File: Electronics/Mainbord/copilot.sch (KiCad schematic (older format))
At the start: 22 parts, among them J33 Screw_Terminal_01x10, J34 Screw_Terminal_01x10, J35 Screw_Terminal_01x10, J36 Screw_Terminal_01x02, J37 Screw_Terminal_01x10, J38 Screw_Terminal_01x10, J39 Screw_Terminal_01x10, U45 74HC165, U46 74HC165, U47 74HC165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

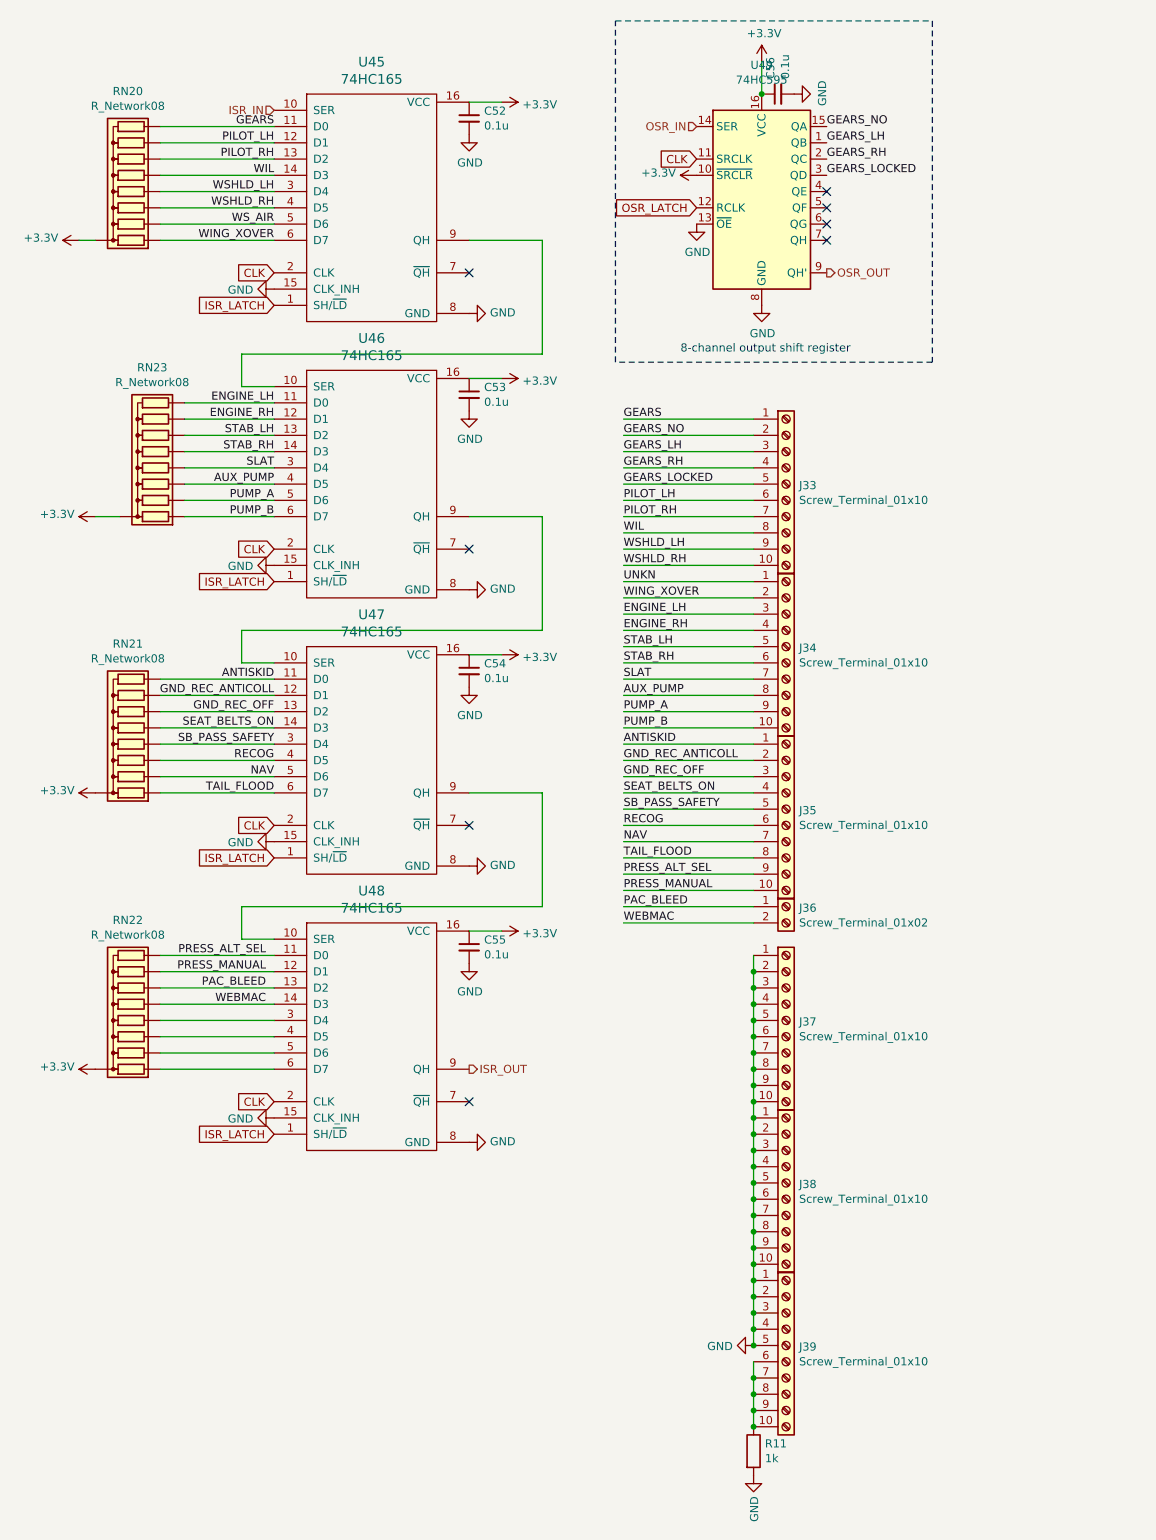
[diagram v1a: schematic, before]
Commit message: Electronics - Minor changes
Resistors to LEDs, transistors
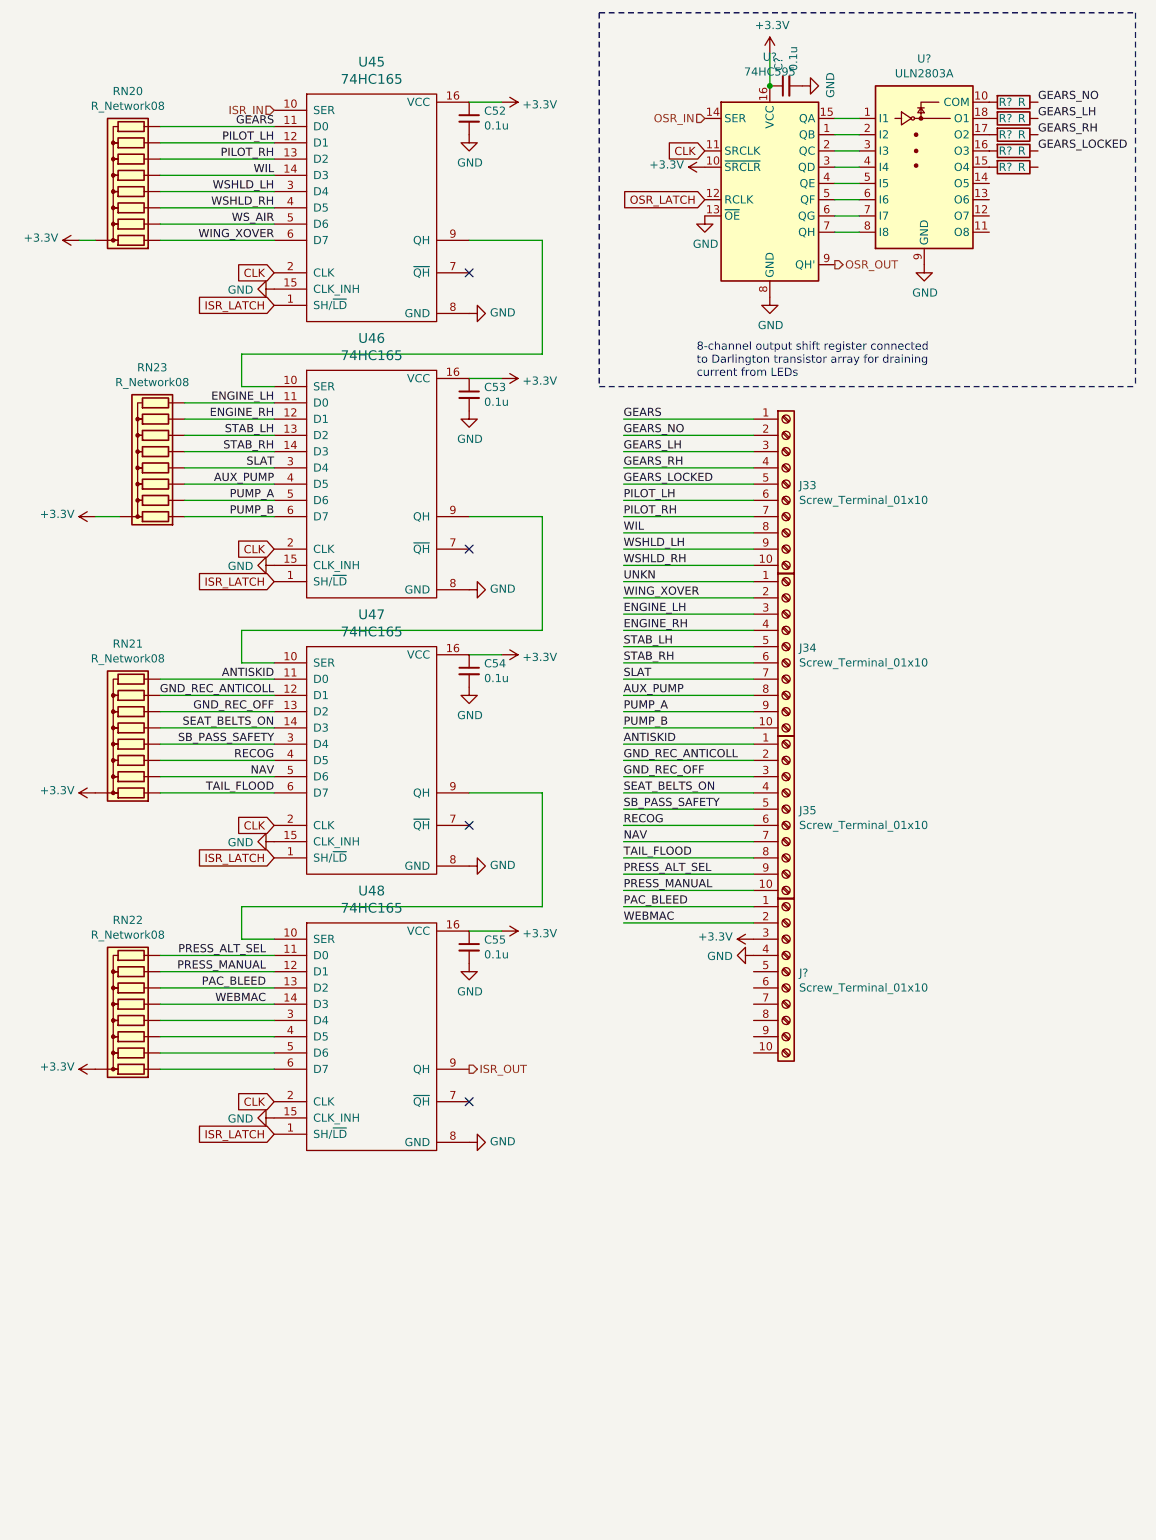
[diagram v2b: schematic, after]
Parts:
- removed C56: 0.1u, symbol Device:C_Small
- removed J36: Screw_Terminal_01x02, symbol Connector:Screw_Terminal_01x02
- removed J37, J38, J39: Screw_Terminal_01x10, symbol Connector:Screw_Terminal_01x10
- removed R11: 1k, symbol Device:R
- removed U49: 74HC595, symbol 74xx:74HC595
- added C?: 0.1u, symbol Device:C_Small
- added J?: Screw_Terminal_01x10, symbol Connector:Screw_Terminal_01x10
- added R? (x5): R, symbol Device:R
- added U?: 74HC595, symbol 74xx:74HC595
- added U?: ULN2803A, symbol Transistor_Array:ULN2803A
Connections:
- net +3V3: now also C?.1, J?.3 (Pin_3), U?.10 (~SRCLR), U?.16 (VCC)
- net CLK: now also U?.11 (SRCLK)
- net GEARS_LH: now also R?.1
- net GEARS_LOCKED: now also R?.1
- net GEARS_NO: now also R?.1
- net GEARS_RH: now also R?.1
- net GND: now also C?.2, J?.4 (Pin_4), U?.13 (~OE), U?.8 (GND), U?.9 (GND)
- net OSR_IN: now also U?.14 (SER)
- net OSR_LATCH: now also U?.12 (RCLK)
- net OSR_OUT: now also U?.9 (QH')
- net PAC_BLEED: now also J?.1 (Pin_1)
- net WEBMAC: now also J?.2 (Pin_2)
- new net: U?.1 (QB), U?.2 (I2)
- new net: U?.1 (I1), U?.15 (QA)
- new net: U?.2 (QC), U?.3 (I3)
- new net: U?.3 (QD), U?.4 (I4)
- new net: U?.4 (QE), U?.5 (I5)
- new net: U?.5 (QF), U?.6 (I6)
- new net: U?.6 (QG), U?.7 (I7)
- new net: U?.7 (QH), U?.8 (I8)
- new net: R?.2, U?.10 (COM)
- new net: R?.2, U?.15 (O4)
- new net: R?.2, U?.16 (O3)
- new net: R?.2, U?.17 (O2)
- new net: R?.2, U?.18 (O1)
- no-connect marks 8 -> 4
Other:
- note added: "8-channel output shift register connected \nto Darlington transistor array for draining \ncurrent from LEDs"
- note removed: "8-channel output shift register"

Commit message: Electronics - Misc works
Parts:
- R? (x4): value R -> 68
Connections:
- net at U?.10 (COM): no longer R?.2
- net at U?.14 (O5): now also R?.2
- net at U?.15 (O4): now also R?.2; no longer R?.2
- net at U?.16 (O3): now also R?.2; no longer R?.2
- net at U?.17 (O2): now also R?.2; no longer R?.2
- net at U?.18 (O1): now also R?.2; no longer R?.2
- no-connect marks 4 -> 5
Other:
- moved on the sheet: R?
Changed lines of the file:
@@
 AR Path="/5DC174D4/5E02571A" Ref="C?"  Part="1"
 AR Path="/5DC31399/5E02571A" Ref="C?"  Part="1"
+AR Path="/5DC2EEA6/5E02571A" Ref="C?"  Part="1"
 F 0 "C?" H 5742 1246 50  0000 L CNN
 F 1 "0.1u" H 5742 1155 50  0000 L CNN
@@
 AR Path="/5DC174D4/5E025721" Ref="#PWR?"  Part="1"
 AR Path="/5DC31399/5E025721" Ref="#PWR?"  Part="1"
+AR Path="/5DC2EEA6/5E025721" Ref="#PWR?"  Part="1"
 F 0 "#PWR?" H 5750 950 50  0001 C CNN
 F 1 "GND" H 5755 1027 50  0000 C CNN
@@
 AR Path="/5DC174D4/5E025728" Ref="U?"  Part="1"
 AR Path="/5DC31399/5E025728" Ref="U?"  Part="1"
+AR Path="/5DC2EEA6/5E025728" Ref="U?"  Part="1"
 F 0 "U?" H 5550 2578 50  0000 C CNN
 F 1 "74HC595" H 5550 2487 50  0000 C CNN
@@
 AR Path="/5DC174D4/5E025730" Ref="#PWR?"  Part="1"
 AR Path="/5DC31399/5E025730" Ref="#PWR?"  Part="1"
+AR Path="/5DC2EEA6/5E025730" Ref="#PWR?"  Part="1"
 F 0 "#PWR?" H 5550 2250 50  0001 C CNN
 F 1 "GND" H 5555 2327 50  0000 C CNN
@@
 AR Path="/5DC174D4/5E025737" Ref="#PWR?"  Part="1"
 AR Path="/5DC31399/5E025737" Ref="#PWR?"  Part="1"
+AR Path="/5DC2EEA6/5E025737" Ref="#PWR?"  Part="1"
 F 0 "#PWR?" H 5150 1750 50  0001 C CNN
 F 1 "GND" H 5155 1827 50  0000 C CNN
@@
 AR Path="/5DC174D4/5E02573E" Ref="#PWR?"  Part="1"
 AR Path="/5DC31399/5E02573E" Ref="#PWR?"  Part="1"
+AR Path="/5DC2EEA6/5E02573E" Ref="#PWR?"  Part="1"
 F 0 "#PWR?" H 5550 850 50  0001 C CNN
 F 1 "+3.3V" H 5565 1173 50  0000 C CNN
@@
 AR Path="/5DC174D4/5E025744" Ref="#PWR?"  Part="1"
 AR Path="/5DC31399/5E025744" Ref="#PWR?"  Part="1"
+AR Path="/5DC2EEA6/5E025744" Ref="#PWR?"  Part="1"
 F 0 "#PWR?" H 5150 1550 50  0001 C CNN
 F 1 "+3.3V" V 5165 1828 50  0000 L CNN
@@
 AR Path="/5DC31399/5E025752" Ref="U?"  Part="1"
 AR Path="/5DC174D4/5E025752" Ref="U?"  Part="1"
+AR Path="/5DC2EEA6/5E025752" Ref="U?"  Part="1"
 F 0 "U?" H 6500 2167 50  0000 C CNN
 F 1 "ULN2803A" H 6500 2076 50  0000 C CNN
@@
 AR Path="/5DC174D4/5E025759" Ref="#PWR?"  Part="1"
 AR Path="/5DC31399/5E025759" Ref="#PWR?"  Part="1"
+AR Path="/5DC2EEA6/5E025759" Ref="#PWR?"  Part="1"
 F 0 "#PWR?" H 6500 2050 50  0001 C CNN
 F 1 "GND" H 6505 2127 50  0000 C CNN
@@
 L Device:R R?
 U 1 1 5E02575F
-P 7050 1300
+P 7050 1400
 AR Path="/5DC33C09/5E02575F" Ref="R?"  Part="1"
 AR Path="/5DC31399/5E02575F" Ref="R?"  Part="1"
 AR Path="/5DC174D4/5E02575F" Ref="R?"  Part="1"
-F 0 "R?" V 7050 1250 50  0000 C CNN
-F 1 "R" V 7050 1350 50  0000 C CNN
-F 2 "" V 6980 1300 50  0001 C CNN
-F 3 "~" H 7050 1300 50  0001 C CNN
-	1    7050 1300
+AR Path="/5DC2EEA6/5E02575F" Ref="R?"  Part="1"
+F 0 "R?" V 7050 1350 50  0000 C CNN
+F 1 "68" V 7050 1450 50  0000 C CNN
+F 2 "" V 6980 1400 50  0001 C CNN
+F 3 "~" H 7050 1400 50  0001 C CNN
+	1    7050 1400
 	0    1    1    0
 $EndComp
@@
 L Device:R R?
 U 1 1 5E025766
-P 7050 1400
+P 7050 1500
 AR Path="/5DC33C09/5E025766" Ref="R?"  Part="1"
 AR Path="/5DC31399/5E025766" Ref="R?"  Part="1"
 AR Path="/5DC174D4/5E025766" Ref="R?"  Part="1"
-F 0 "R?" V 7050 1350 50  0000 C CNN
-F 1 "R" V 7050 1450 50  0000 C CNN
-F 2 "" V 6980 1400 50  0001 C CNN
-F 3 "~" H 7050 1400 50  0001 C CNN
-	1    7050 1400
+AR Path="/5DC2EEA6/5E025766" Ref="R?"  Part="1"
+F 0 "R?" V 7050 1450 50  0000 C CNN
+F 1 "68" V 7050 1550 50  0000 C CNN
+F 2 "" V 6980 1500 50  0001 C CNN
+F 3 "~" H 7050 1500 50  0001 C CNN
+	1    7050 1500
 	0    1    1    0
 $EndComp
@@
 L Device:R R?
 U 1 1 5E02576D
-P 7050 1500
+P 7050 1600
 AR Path="/5DC33C09/5E02576D" Ref="R?"  Part="1"
 AR Path="/5DC31399/5E02576D" Ref="R?"  Part="1"
 AR Path="/5DC174D4/5E02576D" Ref="R?"  Part="1"
-F 0 "R?" V 7050 1450 50  0000 C CNN
-F 1 "R" V 7050 1550 50  0000 C CNN
-F 2 "" V 6980 1500 50  0001 C CNN
-F 3 "~" H 7050 1500 50  0001 C CNN
-	1    7050 1500
+AR Path="/5DC2EEA6/5E02576D" Ref="R?"  Part="1"
+F 0 "R?" V 7050 1550 50  0000 C CNN
+F 1 "68" V 7050 1650 50  0000 C CNN
+F 2 "" V 6980 1600 50  0001 C CNN
+F 3 "~" H 7050 1600 50  0001 C CNN
+	1    7050 1600
 	0    1    1    0
 $EndComp
@@
 L Device:R R?
 U 1 1 5E025774
-P 7050 1600
+P 7050 1700
 AR Path="/5DC33C09/5E025774" Ref="R?"  Part="1"
 AR Path="/5DC31399/5E025774" Ref="R?"  Part="1"
 AR Path="/5DC174D4/5E025774" Ref="R?"  Part="1"
-F 0 "R?" V 7050 1550 50  0000 C CNN
-F 1 "R" V 7050 1650 50  0000 C CNN
-F 2 "" V 6980 1600 50  0001 C CNN
-F 3 "~" H 7050 1600 50  0001 C CNN
-	1    7050 1600
+AR Path="/5DC2EEA6/5E025774" Ref="R?"  Part="1"
+F 0 "R?" V 7050 1650 50  0000 C CNN
+F 1 "68" V 7050 1750 50  0000 C CNN
+F 2 "" V 6980 1700 50  0001 C CNN
+F 3 "~" H 7050 1700 50  0001 C CNN
+	1    7050 1700
 	0    1    1    0
 $EndComp
@@
 L Device:R R?
 U 1 1 5E02577B
-P 7050 1700
+P 7050 1800
 AR Path="/5DC33C09/5E02577B" Ref="R?"  Part="1"
 AR Path="/5DC31399/5E02577B" Ref="R?"  Part="1"
 AR Path="/5DC174D4/5E02577B" Ref="R?"  Part="1"
-F 0 "R?" V 7050 1650 50  0000 C CNN
-F 1 "R" V 7050 1750 50  0000 C CNN
-F 2 "" V 6980 1700 50  0001 C CNN
-F 3 "~" H 7050 1700 50  0001 C CNN
-	1    7050 1700
+AR Path="/5DC2EEA6/5E02577B" Ref="R?"  Part="1"
+F 0 "R?" V 7050 1750 50  0000 C CNN
+F 1 "R" V 7050 1850 50  0000 C CNN
+F 2 "" V 6980 1800 50  0001 C CNN
+F 3 "~" H 7050 1800 50  0001 C CNN
+	1    7050 1800
 	0    1    1    0
 $EndComp
@@
 Wire Notes Line
 	4500 750  4500 3050
+Text Label 7200 1500 0    50   ~ 0
+GEARS_LH
+Text Label 7200 1600 0    50   ~ 0
+GEARS_RH
+Text Label 7200 1700 0    50   ~ 0
+GEARS_LOCKED
 Text Label 7200 1400 0    50   ~ 0
-GEARS_LH
-Text Label 7200 1500 0    50   ~ 0
-GEARS_RH
-Text Label 7200 1600 0    50   ~ 0
-GEARS_LOCKED
-Text Label 7200 1300 0    50   ~ 0
 GEARS_NO
 Wire Notes Line
@@
 	0    1    1    0
 $EndComp
+NoConn ~ 6900 1300
 $EndSCHEMATC
